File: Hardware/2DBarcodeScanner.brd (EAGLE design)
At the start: 44.5 x 22.9 mm, 43 parts, among them J1 BARCODE_ENGINE_CONN, Q1 600mA/40V, Q2 600mA/40V, U1 3.3V

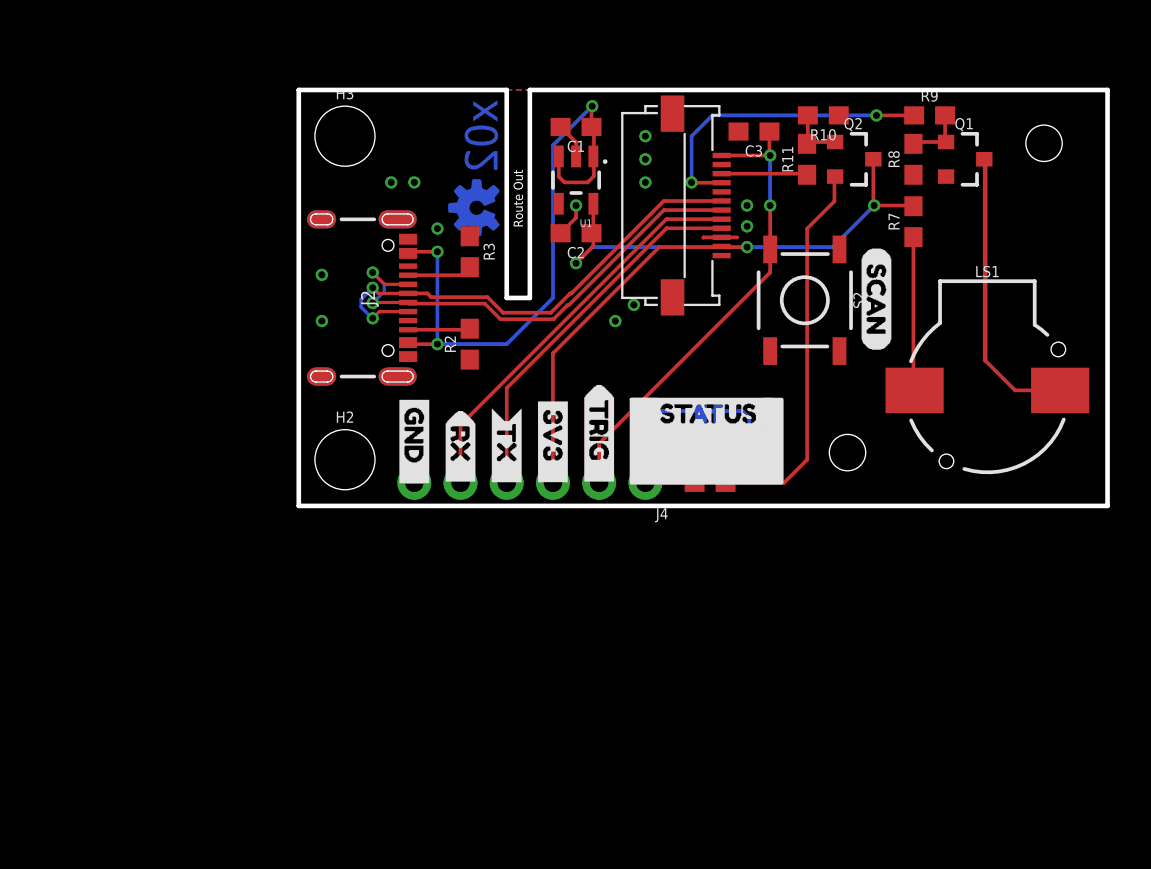
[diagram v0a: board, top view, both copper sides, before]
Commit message: Update SPX design for reds
Changes made:
Switched out 12-pin ribbon cable connector for the one used on the RTK
Added jumper on the buzzer
Added power LED
Updated names/version numbers
Added fiducials
AND updated the barcode scanner footprint/silk
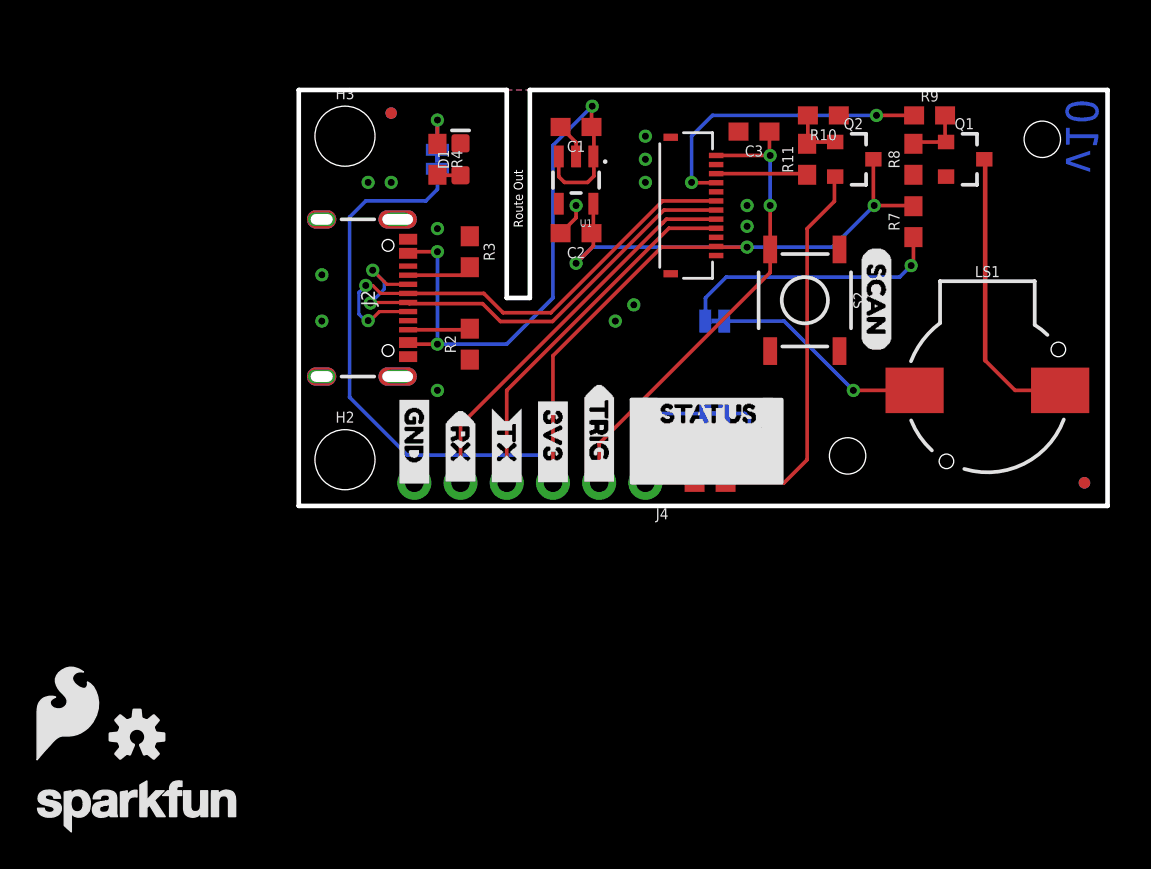
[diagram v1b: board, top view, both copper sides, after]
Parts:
- removed J1: BARCODE_ENGINE_CONN, SparkFun-Connectors:CONN_FPC_BOTTOM_12POS_.5MM_R/A
- removed U$17: (no value), buzzard_labels (2):2D_BARCODE_SCANNER0
- removed U$18: (no value), buzzard_labels (2):BREAKOUT_BOARD1
- removed U$20: (no value), SparkX:SPARKX-MEDIUM
- removed U$21: (no value), SparkFun-Aesthetics:OSHW-LOGO-S_COPPER
- added BUZZ, PWR: JUMPER-SMT_2_NC_TRACE_SILK, SparkFun-Jumpers:SMT-JUMPER_2_NC_TRACE_SILK
- added D1: RED, SparkFun-LED:LED-0603
- added FD1, FD2, FD3, FD4: FIDUCIALUFIDUCIAL, SparkFun-Aesthetics:FIDUCIAL-MICRO
- added J3: (no value), SparkFun-Connectors:FPC_12_0.5MM
- added LOGO1: OSHW-LOGOS, SparkFun-Aesthetics:OSHW-LOGO-S
- added LOGO2: SFE_LOGO_FLAME.2_INCH, SparkFun-Aesthetics:SFE_LOGO_FLAME_.2
- added LOGO3: SFE_LOGO_NAME.1_INCH, SparkFun-Aesthetics:SFE_LOGO_NAME_.1
- added R4: 1k, SparkFun-Resistors:0603
- J2: device SparkFun-Connectors:USB-C-16P -> SparkFun-Connectors:USB-C-16P-2LAYER-PADS
- moved U$1 0.46 mm to (35.8, 11.0)
- moved JP1 0.28 mm to (22.9, 5.08)
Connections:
- new net N$1: BUZZ.2, R7.1
- new net N$6: PWR.1, R4.1
- new net N$9: D1.A, R4.2
- net 3.3V: now also J3.11, PWR.2; no longer J1.P$11
- net BUZZER: now also J3.4; no longer J1.P$4
- net GND: now also D1.C, J3.10; no longer J1.P$10, J1.P$13, J1.P$14
- net N$3: now also BUZZ.1; no longer R7.1
- net RXI: now also J3.8; no longer J1.P$8
- net SCAN_TRIGGER: now also J3.1; no longer J1.P$1
- net SHLD: no longer J2.SHLD5, J2.SHLD6, J2.SHLD7, J2.SHLD8
- net STATUS_LED: now also J3.3; no longer J1.P$3
- net TXO: now also J3.9; no longer J1.P$9
- net USB_N: now also J3.7; no longer J1.P$7
- net USB_P: now also J3.6; no longer J1.P$6
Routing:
- net 3.3V: track 46.5 -> 76.5 mm
- net N$1: track 0.00 -> 14.9 mm, vias 0 -> 1
- net N$3: track 8.45 -> 12.0 mm, vias 0 -> 1
- net N$6: track 0.00 -> 2.95 mm, vias 0 -> 1
- net GND: track 5.74 -> 3.85 mm, vias 13 -> 14
- net N$9: track 0.00 -> 1.28 mm
- net USB_P: track 26.6 -> 27.2 mm
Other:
- board text added: "Original Design by: Nick Poole Revised by: Priyanka Makin"
- board text added: "v10"
- board text removed: "x02"

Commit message: Update silkscreen
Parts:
- removed U$10, U$11: (no value), buzzard_labels (32):TX__2
- removed U$12, U$13: (no value), buzzard_labels (32):RX__1
- removed U$14, U$15: (no value), buzzard_labels (32):GND__0
- removed U$5: (no value), buzzard_labels (32):TRIG__4
- removed U$6, U$9: (no value), buzzard_labels (32):3V3__3
- removed U$7: (no value), buzzard_labels:SCAN4
- added U$16, U$23: (no value), output:3#3V0
- added U$17, U$18: (no value), output:2D_BARCODE0
- added U$19: (no value), output:SCANNER0
- added U$20: (no value), output:SCANNER_BREAKOUT0
- added U$21: (no value), output:#STAT_#0
- added U$22: (no value), output:BUZZ0
- added U$24, U$25: (no value), output:#TRIG_#0
- added U$26, U$27: (no value), output:#TX_#0
- added U$28, U$29: (no value), output:#3#3V_#0
- added U$30, U$31: (no value), output:#RX_#0
- added U$32, U$33: (no value), output:#GND_#0
- LOGO2: value SFE_LOGO_FLAME.2_INCH -> SFE_LOGO_FLAME.1_INCH; device SparkFun-Aesthetics:SFE_LOGO_FLAME_.2 -> SparkFun-Aesthetics:SFE_LOGO_FLAME_.1
- U$2: device buzzard_labels:STATUS3 -> output:#STAT_#0
- U$3: device buzzard_labels (32):STAT__5 -> output:STAT0
- U$4: device buzzard_labels (32):TRIG__4 -> output:#SCAN#0
- U$8: device buzzard_labels (33):LED0 -> output:STAT0
- moved LOGO3 47.4 mm to (20.3, 20.8), flipped to the bottom
- moved LOGO2 35.0 mm to (14.6, 10.4)
- moved LOGO1 26.7 mm to (17.8, -12.7), flipped to the bottom
- moved U$4 16.8 mm to (31.6, 14.1), flipped to the top
- moved U$8 3.78 mm to (26.2, 6.99)
- moved U$3 3.07 mm to (21.0, 4.45), flipped to the top, turned to 0 degrees
- moved BUZZ 2.84 mm to (25.4, 11.4)
- moved U$2 2.04 mm to (19.1, 7.11), turned to 270 degrees
- moved D2 1.02 mm to (23.6, 3.17)
- moved R1 0.89 mm to (23.5, 1.27)
- moved JP1 0.64 mm to (23.5, 5.08)
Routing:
- net N$1: track 14.9 -> 11.6 mm
- net N$4: track 21.2 -> 20.3 mm
- net STATUS_OUT: track 9.58 -> 10.4 mm
- net GND: vias 14 -> 13

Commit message: Silkscreen
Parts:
- moved LOGO1 26.7 mm to (19.8, 14.0)
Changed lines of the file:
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@@
 <?xml version="1.0" encoding="utf-8"?>
 <!DOCTYPE eagle SYSTEM "eagle.dtd">
-<eagle version="9.6.2">
+<eagle version="9.5.2">
 <drawing>
 <settings>
@@
 <attribute name="VALUE" x="25.4" y="10.287" size="0.6096" layer="28" font="vector" ratio="20" rot="MR0" align="top-center"/>
 </element>
-<element name="LOGO1" library="SparkFun-Aesthetics" package="OSHW-LOGO-S" value="OSHW-LOGOS" x="17.78" y="-12.7" smashed="yes" rot="MR0"/>
+<element name="LOGO1" library="SparkFun-Aesthetics" package="OSHW-LOGO-S" value="OSHW-LOGOS" x="19.812" y="13.97" smashed="yes" rot="MR0"/>
 <element name="LOGO2" library="SparkFun-Aesthetics" package="SFE_LOGO_FLAME_.1" value="SFE_LOGO_FLAME.1_INCH" x="14.605" y="10.414" smashed="yes"/>
 <element name="LOGO3" library="SparkFun-Aesthetics" package="SFE_LOGO_NAME_.1" value="SFE_LOGO_NAME.1_INCH" x="20.32" y="20.828" smashed="yes" rot="MR0"/>

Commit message: Update silkscreen
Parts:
- removed U$22: (no value), output:BUZZ0
- removed U$23: (no value), output:3#3V0
- removed U$8: (no value), output:STAT0
- added U$5: (no value), output:#BUZZ#0
- added U$6: (no value), output:#STAT#0
- added U$7: (no value), output:#3#3V#0
- moved JP1 2.92 mm to (26.4, 5.21)
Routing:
- net STATUS_OUT: track 10.4 -> 13.3 mm
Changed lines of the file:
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@@
 <?xml version="1.0" encoding="utf-8"?>
 <!DOCTYPE eagle SYSTEM "eagle.dtd">
-<eagle version="9.5.2">
+<eagle version="9.6.2">
 <drawing>
 <settings>
@@
 <layer number="19" name="Unrouted" color="6" fill="1" visible="yes" active="yes"/>
 <layer number="20" name="Dimension" color="24" fill="1" visible="yes" active="yes"/>
-<layer number="21" name="tPlace" color="16" fill="1" visible="yes" active="yes"/>
+<layer number="21" name="tPlace" color="16" fill="1" visible="no" active="yes"/>
 <layer number="22" name="bPlace" color="14" fill="1" visible="yes" active="yes"/>
 <layer number="23" name="tOrigins" color="15" fill="1" visible="yes" active="yes"/>
@@
 <attribute name="VALUE" x="20.32" y="3.302" size="0.6096" layer="27" font="vector" ratio="20" rot="R180"/>
 </element>
-<element name="JP1" library="SparkFun-Jumpers" package="SMT-JUMPER_2_NC_TRACE_SILK" package3d_urn="urn:adsk.eagle:package:39281/1" value="JUMPER-SMT_2_NC_TRACE_SILK" x="23.495" y="5.08" smashed="yes" rot="MR0">
-<attribute name="NAME" x="23.495" y="6.223" size="0.6096" layer="26" font="vector" ratio="20" rot="MR0" align="bottom-center"/>
-<attribute name="VALUE" x="23.495" y="3.937" size="0.6096" layer="28" font="vector" ratio="20" rot="MR0" align="top-center"/>
+<element name="JP1" library="SparkFun-Jumpers" package="SMT-JUMPER_2_NC_TRACE_SILK" package3d_urn="urn:adsk.eagle:package:39281/1" value="JUMPER-SMT_2_NC_TRACE_SILK" x="26.416" y="5.207" smashed="yes" rot="MR0">
+<attribute name="NAME" x="26.416" y="6.35" size="0.6096" layer="26" font="vector" ratio="20" rot="MR0" align="bottom-center"/>
+<attribute name="VALUE" x="26.416" y="4.064" size="0.6096" layer="28" font="vector" ratio="20" rot="MR0" align="top-center"/>
 </element>
 <element name="FD1" library="SparkFun-Aesthetics" package="FIDUCIAL-MICRO" value="FIDUCIALUFIDUCIAL" x="5.08" y="21.59" smashed="yes"/>
@@
 <element name="U$19" library="output" package="SCANNER0" value="" x="16.51" y="9.652" smashed="yes"/>
 <element name="U$21" library="output" package="#STAT_#0" value="" x="19.05" y="7.112" smashed="yes" rot="MR270"/>
-<element name="U$22" library="output" package="BUZZ0" value="" x="27.94" y="13.462" smashed="yes" rot="MR0"/>
-<element name="U$23" library="output" package="3#3V0" value="" x="5.588" y="21.463" smashed="yes" rot="MR270"/>
-<element name="U$8" library="output" package="STAT0" value="" x="26.162" y="6.985" smashed="yes" rot="MR0"/>
 <element name="U$24" library="output" package="#TRIG_#0" value="" x="16.51" y="6.477" smashed="yes" rot="R270"/>
 <element name="U$25" library="output" package="#TRIG_#0" value="" x="16.51" y="6.477" smashed="yes" rot="MR270"/>
@@
 <element name="U$33" library="output" package="#GND_#0" value="" x="6.35" y="6.096" smashed="yes" rot="MR270"/>
 <element name="U$4" library="output" package="#SCAN#0" value="" x="31.623" y="14.097" smashed="yes" rot="R270"/>
+<element name="U$5" library="output" package="#BUZZ#0" value="" x="24.511" y="11.43" smashed="yes" rot="MR0"/>
+<element name="U$6" library="output" package="#STAT#0" value="" x="25.654" y="5.207" smashed="yes" rot="MR0"/>
+<element name="U$7" library="output" package="#3#3V#0" value="" x="7.62" y="18.288" smashed="yes" rot="MR270"/>
 </elements>
 <signals>
@@
 <via x="5.08" y="17.78" extent="1-16" drill="0.381"/>
 <via x="3.81" y="17.78" extent="1-16" drill="0.381"/>
-<via x="7.62" y="15.24" extent="1-16" drill="0.381"/>
+<via x="10.16" y="16.51" extent="1-16" drill="0.381"/>
 <via x="1.27" y="12.7" extent="1-16" drill="0.381"/>
 <via x="1.27" y="10.16" extent="1-16" drill="0.381"/>
@@
 <contactref element="JP1" pad="2"/>
 <contactref element="J4" pad="1"/>
-<wire x1="22.9743" y1="5.08" x2="20.701" y2="5.08" width="0.2032" layer="16"/>
-<wire x1="20.701" y1="5.08" x2="19.05" y2="3.429" width="0.2032" layer="16"/>
+<wire x1="25.8953" y1="5.207" x2="20.828" y2="5.207" width="0.2032" layer="16"/>
+<wire x1="20.828" y1="5.207" x2="19.05" y2="3.429" width="0.2032" layer="16"/>
 <wire x1="19.05" y1="1.27" x2="19.05" y2="3.429" width="0.2032" layer="16"/>
 <wire x1="22.645" y1="1.27" x2="19.05" y2="1.27" width="0.2032" layer="1"/>
@@
 <contactref element="JP1" pad="1"/>
 <contactref element="D2" pad="A"/>
-<wire x1="25.019" y1="5.08" x2="24.0157" y2="5.08" width="0.2032" layer="16"/>
+<wire x1="26.9367" y1="5.207" x2="26.924" y2="5.1943" width="0.2032" layer="16"/>
+<wire x1="26.924" y1="5.1943" x2="26.924" y2="3.683" width="0.2032" layer="16"/>
+<wire x1="26.924" y1="3.683" x2="26.543" y2="3.302" width="0.2032" layer="16"/>
+<wire x1="26.543" y1="3.302" x2="25.908" y2="3.302" width="0.2032" layer="16"/>
 <wire x1="25.781" y1="3.175" x2="25.908" y2="3.302" width="0.2032" layer="1"/>
 <wire x1="25.781" y1="3.175" x2="24.499" y2="3.175" width="0.2032" layer="1"/>
 <via x="25.908" y="3.302" extent="1-16" drill="0.381"/>
-<wire x1="25.908" y1="3.302" x2="25.908" y2="4.191" width="0.2032" layer="16"/>
-<wire x1="25.908" y1="4.191" x2="25.019" y2="5.08" width="0.2032" layer="16"/>
 </signal>
 <signal name="N$1">

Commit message: Ran schematic/board checklists
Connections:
- removed net SHLD: J2.SHLD1, J2.SHLD2, J2.SHLD3, J2.SHLD4
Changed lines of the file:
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@@
 <?xml version="1.0" encoding="utf-8"?>
 <!DOCTYPE eagle SYSTEM "eagle.dtd">
-<eagle version="9.6.2">
+<eagle version="9.5.2">
 <drawing>
 <settings>
-<setting alwaysvectorfont="yes"/>
+<setting alwaysvectorfont="no"/>
 <setting verticaltext="up"/>
 </settings>
@@
 <layer number="19" name="Unrouted" color="6" fill="1" visible="yes" active="yes"/>
 <layer number="20" name="Dimension" color="24" fill="1" visible="yes" active="yes"/>
-<layer number="21" name="tPlace" color="16" fill="1" visible="no" active="yes"/>
+<layer number="21" name="tPlace" color="16" fill="1" visible="yes" active="yes"/>
 <layer number="22" name="bPlace" color="14" fill="1" visible="yes" active="yes"/>
 <layer number="23" name="tOrigins" color="15" fill="1" visible="yes" active="yes"/>
@@
 <contactref element="Q2" pad="3"/>
 <contactref element="J4" pad="3"/>
-<wire x1="24.638" y1="14.224" x2="19.939" y2="14.224" width="0.2032" layer="1"/>
 <wire x1="19.939" y1="14.224" x2="13.97" y2="8.255" width="0.2032" layer="1"/>
 <wire x1="13.97" y1="8.255" x2="13.97" y2="1.27" width="0.2032" layer="1"/>
@@
 <wire x1="2.794" y1="15.875" x2="2.794" y2="5.969" width="0.2032" layer="16"/>
 <wire x1="2.794" y1="5.969" x2="5.969" y2="2.794" width="0.2032" layer="16"/>
-<wire x1="24.638" y1="14.224" x2="22.94" y2="14.26" width="0" layer="19" extent="1-1"/>
+<wire x1="24.638" y1="14.224" x2="22.976" y2="14.224" width="0.2032" layer="1"/>
+<wire x1="22.976" y1="14.224" x2="22.94" y2="14.26" width="0.2032" layer="1"/>
+<wire x1="22.94" y1="14.26" x2="22.904" y2="14.224" width="0.2032" layer="1"/>
+<wire x1="22.904" y1="14.224" x2="19.939" y2="14.224" width="0.2032" layer="1"/>
 </signal>
 <signal name="TXO">
@@
 <wire x1="20.205" y1="15.76" x2="20.0025" y2="15.5575" width="0.2032" layer="1"/>
 </signal>
-<signal name="SHLD" airwireshidden="yes">
-<contactref element="J2" pad="SHLD2"/>
-<contactref element="J2" pad="SHLD4"/>
-<contactref element="J2" pad="SHLD1"/>
-<contactref element="J2" pad="SHLD3"/>
-<wire x1="1.255" y1="15.748" x2="5.435" y2="15.748" width="0" layer="19" extent="1-1"/>
-<wire x1="5.435" y1="7.112" x2="5.435" y2="15.748" width="0" layer="19" extent="1-1"/>
-<wire x1="1.255" y1="7.112" x2="5.435" y2="7.112" width="0" layer="19" extent="1-1"/>
-</signal>
 <signal name="5V">
